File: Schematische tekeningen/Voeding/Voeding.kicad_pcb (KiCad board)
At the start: 2 copper layers, 66.2 x 52.9 mm, 66 parts, among them J1 VCC, J2 GND, J3 GNDS, J4 +3.3V_ISO, J5 +3.3V, J6 GND, J7 MCU_RST, J8 Fault_signals, Q1 FDN340P, Q2 2N7002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

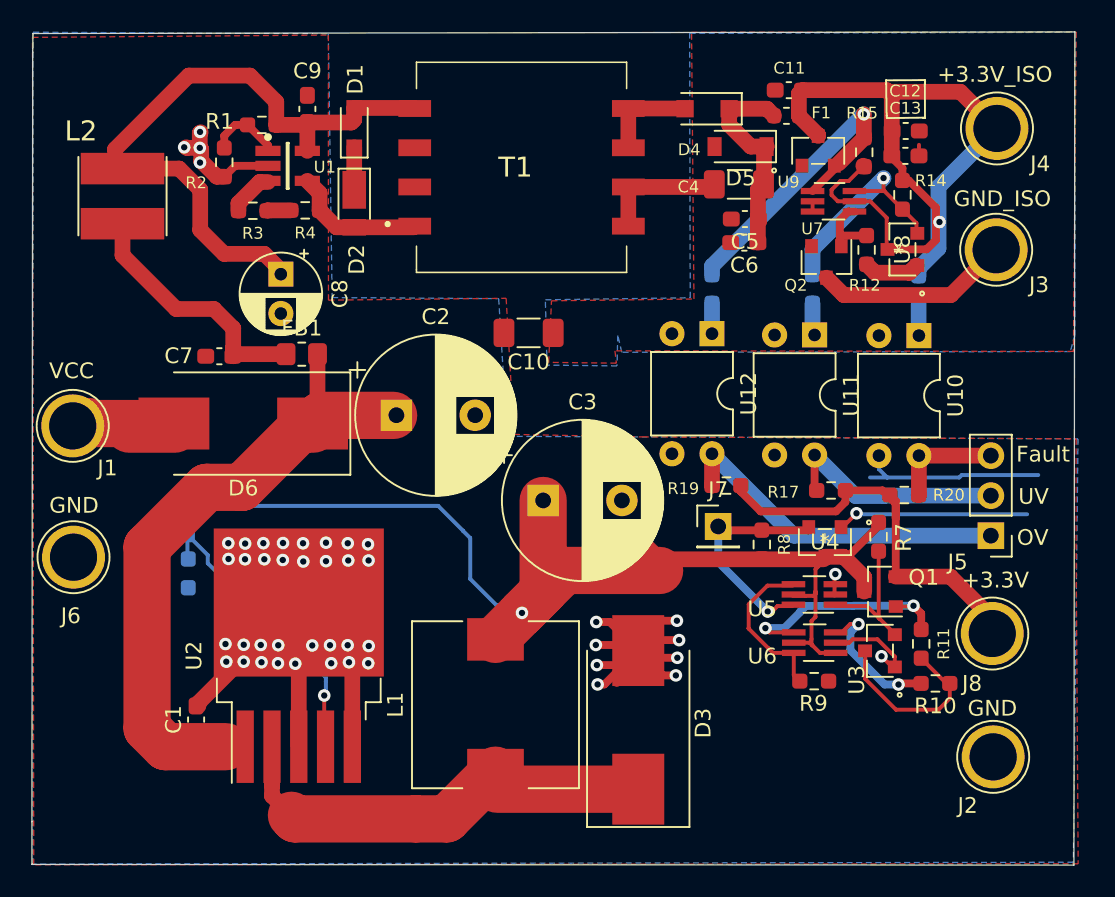
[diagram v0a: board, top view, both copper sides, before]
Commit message: Gaten toevoegen aan printplaat voeding
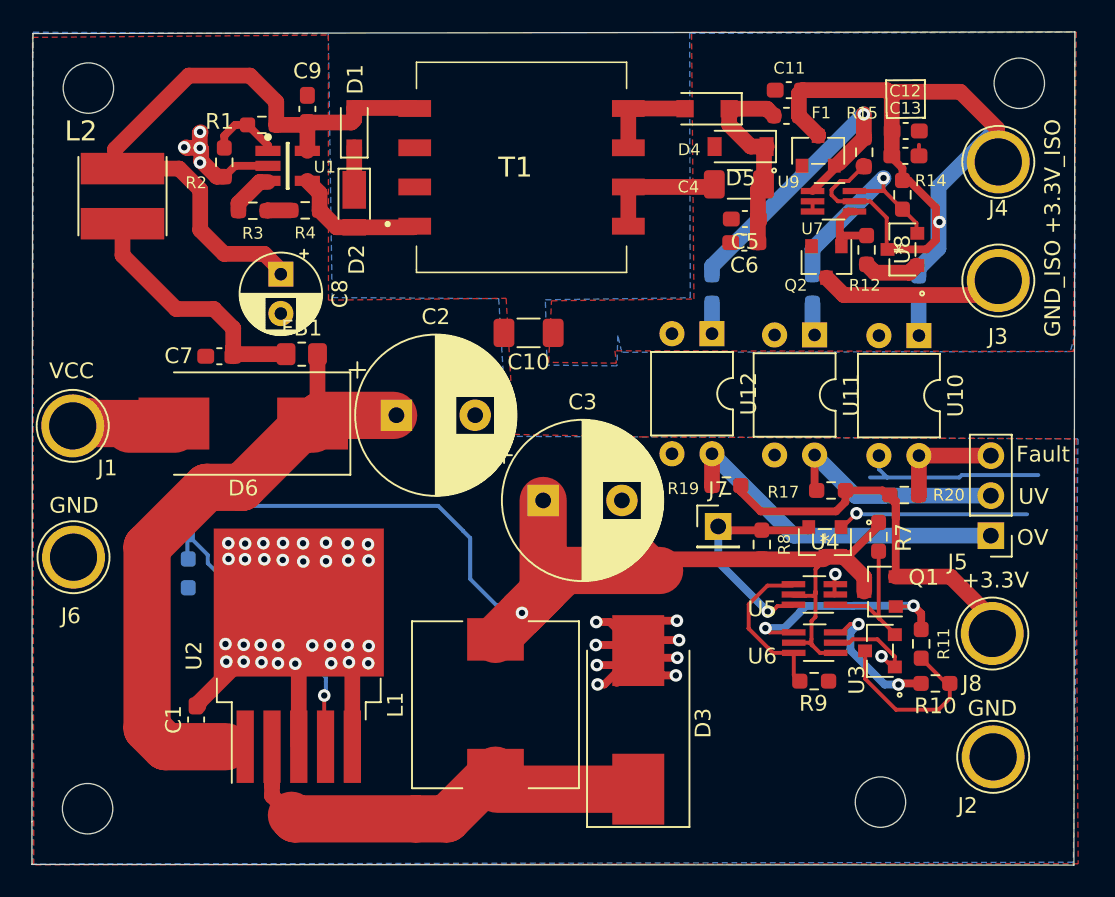
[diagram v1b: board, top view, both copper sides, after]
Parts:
- added REF**: MountingHole_3.2mm_M3, MountingHole:MountingHole_3.2mm_M3, F.Cu at (144.8, 43.4)
- added REF**: MountingHole_3.2mm_M3, MountingHole:MountingHole_3.2mm_M3, F.Cu at (136.0, 89.0)
- added REF**: MountingHole_3.2mm_M3, MountingHole:MountingHole_3.2mm_M3, F.Cu at (85.7, 89.4)
- added REF**: MountingHole_3.2mm_M3, MountingHole:MountingHole_3.2mm_M3, F.Cu at (85.7, 43.7)
- moved J4 2.13 mm to (143.5, 48.4)
- moved J3 1.96 mm to (143.5, 55.9)
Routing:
- net +3.3VP: track 51.5 -> 53.6 mm
- net Net-(J3-Pad1): track 12.4 -> 11.7 mm

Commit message: Gerbers geexporteerd voor de voeding printplaat
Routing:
- net V_FB: track 19.1 -> 23.9 mm
- net +3V3: track 86.8 -> 88.7 mm
- net GND: track 144.7 -> 143.7 mm, vias 47 -> 49
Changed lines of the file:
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@@
-(kicad_pcb (version 20171130) (host pcbnew 5.1.12-84ad8e8a86~92~ubuntu20.04.1)
+(kicad_pcb (version 20171130) (host pcbnew 5.1.10)
   (general
     (thickness 1.6)
     (drawings 25)
-    (tracks 429)
+    (tracks 432)
     (zones 0)
     (modules 70)
@@
   )
   (setup
-    (last_trace_width 1)
+    (last_trace_width 0.25)
     (user_trace_width 0.5)
     (user_trace_width 1)
@@
     (pcbplotparams
       (layerselection 0x010fc_ffffffff)
-      (usegerberextensions false)
+      (usegerberextensions true)
       (usegerberattributes true)
       (usegerberadvancedattributes true)
-      (creategerberjobfile true)
+      (creategerberjobfile false)
       (excludeedgelayer true)
-      (linewidth 0.100000)
+      (linewidth 0.150000)
       (plotframeref false)
       (viasonmask false)
@@
       (psa4output false)
       (plotreference true)
-      (plotvalue true)
+      (plotvalue false)
       (plotinvisibletext false)
       (padsonsilk false)
-      (subtractmaskfromsilk false)
+      (subtractmaskfromsilk true)
       (outputformat 1)
       (mirror false)
-      (drillshape 1)
+      (drillshape 0)
       (scaleselection 1)
-      (outputdirectory ""))
+      (outputdirectory "Gerbers/"))
   )
   (net 0 "")
@@
       (effects (font (size 1 1) (thickness 0.15)))
     )
+    (fp_circle (center 0 0) (end 3.2 0) (layer Cmts.User) (width 0.15))
+    (fp_circle (center 0 0) (end 3.45 0) (layer F.CrtYd) (width 0.05))
     (fp_text user %R (at 0.3 0) (layer F.Fab)
       (effects (font (size 1 1) (thickness 0.15)))
     )
-    (fp_circle (center 0 0) (end 3.2 0) (layer Cmts.User) (width 0.15))
-    (fp_circle (center 0 0) (end 3.45 0) (layer F.CrtYd) (width 0.05))
     (pad 1 np_thru_hole circle (at 0 0) (size 3.2 3.2) (drill 3.2) (layers *.Cu *.Mask))
   )
@@
       (effects (font (size 0.5 0.5) (thickness 0.08)))
     )
-    (pad 2 smd roundrect (at 1 0) (size 1.2 1.4) (layers F.Cu F.Paste F.Mask) (roundrect_rratio 0.208333)
+    (pad 2 smd roundrect (at 1 0) (size 1.2 1.4) (layers F.Cu F.Paste F.Mask) (roundrect_rratio 0.2083325)
       (net 32 VDC))
-    (pad 1 smd roundrect (at -1 0) (size 1.2 1.4) (layers F.Cu F.Paste F.Mask) (roundrect_rratio 0.208333)
+    (pad 1 smd roundrect (at -1 0) (size 1.2 1.4) (layers F.Cu F.Paste F.Mask) (roundrect_rratio 0.2083325)
       (net 11 "Net-(C7-Pad1)"))
     (model ${KISYS3DMOD}/Resistor_SMD.3dshapes/R_0805_2012Metric.wrl
@@
       (effects (font (size 0.8 0.8) (thickness 0.12)))
     )
-    (pad 2 smd roundrect (at 1.5625 0 180) (size 1.325 1.8) (layers F.Cu F.Paste F.Mask) (roundrect_rratio 0.188679)
+    (pad 2 smd roundrect (at 1.5625 0 180) (size 1.325 1.8) (layers F.Cu F.Paste F.Mask) (roundrect_rratio 0.1886784905660377)
       (net 1 GND))
-    (pad 1 smd roundrect (at -1.5625 0 180) (size 1.325 1.8) (layers F.Cu F.Paste F.Mask) (roundrect_rratio 0.188679)
+    (pad 1 smd roundrect (at -1.5625 0 180) (size 1.325 1.8) (layers F.Cu F.Paste F.Mask) (roundrect_rratio 0.1886784905660377)
       (net 30 Earth))
     (model ${KISYS3DMOD}/Capacitor_SMD.3dshapes/C_1206_3216Metric.wrl
@@
       (effects (font (size 0.8 0.8) (thickness 0.12)))
     )
-    (pad 2 smd roundrect (at 1.5625 0 180) (size 1.325 1.8) (layers F.Cu F.Paste F.Mask) (roundrect_rratio 0.188679)
+    (pad 2 smd roundrect (at 1.5625 0 180) (size 1.325 1.8) (layers F.Cu F.Paste F.Mask) (roundrect_rratio 0.1886784905660377)
       (net 30 Earth))
-    (pad 1 smd roundrect (at -1.5625 0 180) (size 1.325 1.8) (layers F.Cu F.Paste F.Mask) (roundrect_rratio 0.188679)
+    (pad 1 smd roundrect (at -1.5625 0 180) (size 1.325 1.8) (layers F.Cu F.Paste F.Mask) (roundrect_rratio 0.1886784905660377)
       (net 13 "Net-(C4-Pad1)"))
     (model ${KISYS3DMOD}/Capacitor_SMD.3dshapes/C_1206_3216Metric.wrl
@@
   (gr_line (start 82.13852 90.25636) (end 82.13852 92.96908) (layer Edge.Cuts) (width 0.05))
   (gr_line (start 82.18932 41.41724) (end 82.13852 90.25636) (layer Edge.Cuts) (width 0.05))
+  (via (at 99.95916 80.20558) (size 0.8) (drill 0.4) (layers F.Cu B.Cu) (net 1) (status 30))
+  (via (at 98.84664 79.05496) (size 0.8) (drill 0.4) (layers F.Cu B.Cu) (net 1) (status 30))
   (via (at 103.52024 79.10576) (size 0.8) (drill 0.4) (layers F.Cu B.Cu) (net 1) (status 30))
   (via (at 103.48976 80.19796) (size 0.8) (drill 0.4) (layers F.Cu B.Cu) (net 1) (status 30))
@@
   (segment (start 92.71 82.715) (end 99.079 76.346) (width 1) (layer F.Cu) (net 1) (status 30))
   (segment (start 92.71 82.91288) (end 92.71 82.715) (width 1) (layer F.Cu) (net 1) (status 30))
-  (via (at 133.14172 74.53884) (size 0.8) (drill 0.4) (layers F.Cu B.Cu) (net 1))
+  (via (at 133.13156 74.6252) (size 0.8) (drill 0.4) (layers F.Cu B.Cu) (net 1))
   (segment (start 133.09 74.7864) (end 133.1214 74.755) (width 0.25) (layer F.Cu) (net 1))
   (segment (start 133.09 75.92) (end 133.09 74.7864) (width 0.25) (layer F.Cu) (net 1))
@@
   (segment (start 134.236081 78.679159) (end 134.02525 78.88999) (width 0.25) (layer F.Cu) (net 1))
   (segment (start 135.816279 78.679159) (end 134.236081 78.679159) (width 0.25) (layer F.Cu) (net 1))
-  (segment (start 136.916279 79.779159) (end 135.816279 78.679159) (width 0.25) (layer F.Cu) (net 1))
-  (segment (start 136.916279 80.435559) (end 136.916279 79.779159) (width 0.25) (layer F.Cu) (net 1))
   (via (at 136.070782 79.756) (size 0.8) (drill 0.4) (layers F.Cu B.Cu) (net 1))
   (segment (start 136.750341 80.435559) (end 136.070782 79.756) (width 0.25) (layer F.Cu) (net 1))
   (segment (start 136.916279 80.435559) (end 136.750341 80.435559) (width 0.25) (layer F.Cu) (net 1))
+  (segment (start 136.070782 78.933662) (end 135.816279 78.679159) (width 0.25) (layer F.Cu) (net 1))
+  (segment (start 136.070782 79.756) (end 136.070782 78.933662) (width 0.25) (layer F.Cu) (net 1))
   (segment (start 134.914999 48.614999) (end 134.975 48.675) (width 1) (layer F.Cu) (net 2) (status 30))
   (segment (start 136.725 47.1059) (end 136.725 47.2) (width 0.25) (layer F.Cu) (net 2) (status 10))
@@
   (segment (start 93.301641 73.328361) (end 93.301641 73.850321) (width 0.25) (layer B.Cu) (net 10))
   (segment (start 92.00896 72.03568) (end 93.301641 73.328361) (width 0.25) (layer B.Cu) (net 10) (status 10))
-  (segment (start 100.79736 81.34604) (end 100.79736 82.13852) (width 0.25) (layer B.Cu) (net 10))
-  (segment (start 95.03664 75.58532) (end 95.6056 75.58532) (width 0.25) (layer B.Cu) (net 10))
-  (segment (start 93.301641 73.850321) (end 95.03664 75.58532) (width 0.25) (layer B.Cu) (net 10))
-  (segment (start 100.79736 81.095998) (end 100.79736 81.34604) (width 0.25) (layer B.Cu) (net 10))
-  (segment (start 99.208759 79.507397) (end 100.79736 81.095998) (width 0.25) (layer B.Cu) (net 10))
-  (segment (start 99.208759 79.188479) (end 99.208759 79.507397) (width 0.25) (layer B.Cu) (net 10))
-  (segment (start 95.6056 75.58532) (end 99.208759 79.188479) (width 0.25) (layer B.Cu) (net 10))
   (via (at 100.69576 82.2452) (size 0.8) (drill 0.4) (layers F.Cu B.Cu) (net 10))
   (segment (start 100.79736 82.1436) (end 100.69576 82.2452) (width 0.25) (layer B.Cu) (net 10))
@@
   (segment (start 100.69576 85.41276) (end 100.779 85.496) (width 0.25) (layer F.Cu) (net 10) (status 30))
   (segment (start 100.69576 82.2452) (end 100.69576 85.41276) (width 0.25) (layer F.Cu) (net 10) (status 20))
+  (segment (start 94.18066 74.72934) (end 94.18066 76.43876) (width 0.25) (layer B.Cu) (net 10))
+  (segment (start 93.301641 73.850321) (end 94.18066 74.72934) (width 0.25) (layer B.Cu) (net 10))
+  (segment (start 94.18066 76.43876) (end 92.76334 77.85608) (width 0.25) (layer B.Cu) (net 10))
+  (segment (start 92.76334 77.85608) (end 92.76334 80.99552) (width 0.25) (layer B.Cu) (net 10))
+  (segment (start 94.01302 82.2452) (end 100.69576 82.2452) (width 0.25) (layer B.Cu) (net 10))
+  (segment (start 92.76334 80.99552) (end 94.01302 82.2452) (width 0.25) (layer B.Cu) (net 10))
   (segment (start 95.03156 60.579) (end 94.89948 60.71108) (width 1) (layer F.Cu) (net 11))
   (segment (start 98.26904 60.579) (end 95.03156 60.579) (width 1) (layer F.Cu) (net 11))
@@
   (segment (start 130.50108 78.8924) (end 131.51108 78.8924) (width 0.25) (layer F.Cu) (net 31))
   (segment (start 132.16108 79.5424) (end 131.69394 79.07526) (width 0.25) (layer F.Cu) (net 31))
+  (segment (start 134.89444 79.5424) (end 135.02628 79.41056) (width 0.25) (layer F.Cu) (net 31))
+  (segment (start 133.16108 79.5424) (end 134.89444 79.5424) (width 0.25) (layer F.Cu) (net 31))
   (segment (start 93.56812 85.496) (end 92.71 84.63788) (width 1) (layer F.Cu) (net 32) (status 20))
   (segment (start 94.4622 85.496) (end 93.56812 85.496) (width 1) (layer F.Cu) (net 32))
